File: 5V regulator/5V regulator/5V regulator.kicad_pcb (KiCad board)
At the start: 2 copper layers, 8 parts, among them J1 9V Vhod, J2 5V Izhod, U1 LM7805_TO220

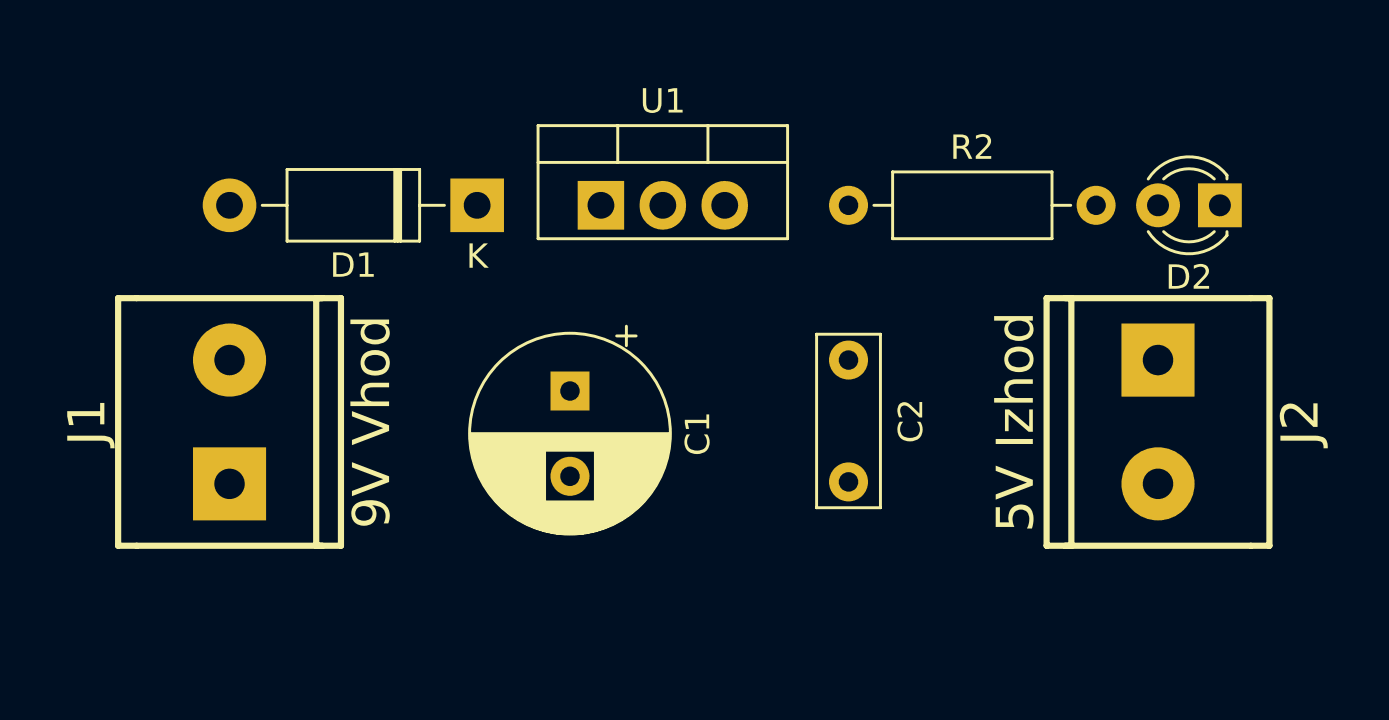
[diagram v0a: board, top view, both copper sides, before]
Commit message: 5v regulator pcb
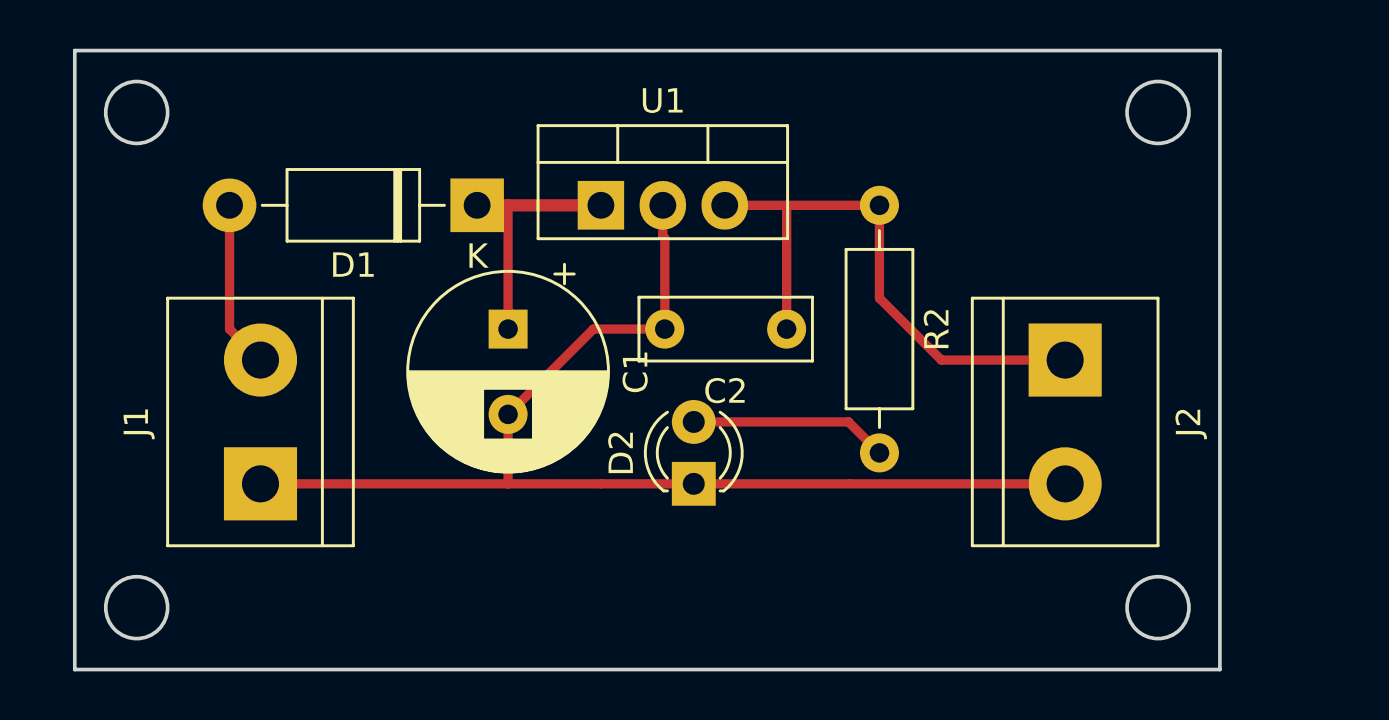
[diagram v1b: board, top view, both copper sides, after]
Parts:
- J1, J2: footprint w_conn_screw:mors_2p -> TerminalBlock:TerminalBlock_bornier-2_P5.08mm
- moved D2 24.4 mm to (144.8, 85.1), turned to 90 degrees
- moved J2 4.58 mm to (160.0, 80.0)
- moved C1 3.59 mm to (137.2, 78.7)
- moved J1 2.84 mm to (127.0, 85.1)
- moved C2 2.84 mm to (148.6, 78.7), turned to 180 degrees
- moved R2 1.27 mm to (152.4, 73.7), turned to 270 degrees
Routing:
- net Net-(C1-Pad2): track 0.00 -> 50.0 mm
- net /5V: track 0.00 -> 23.9 mm
- net Net-(C1-Pad1): track 0.00 -> 10.2 mm
- net Net-(D2-Pad2): track 0.00 -> 8.15 mm
- net /9V: track 0.00 -> 6.88 mm
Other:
- board outline added: 47 x 25.4 mm

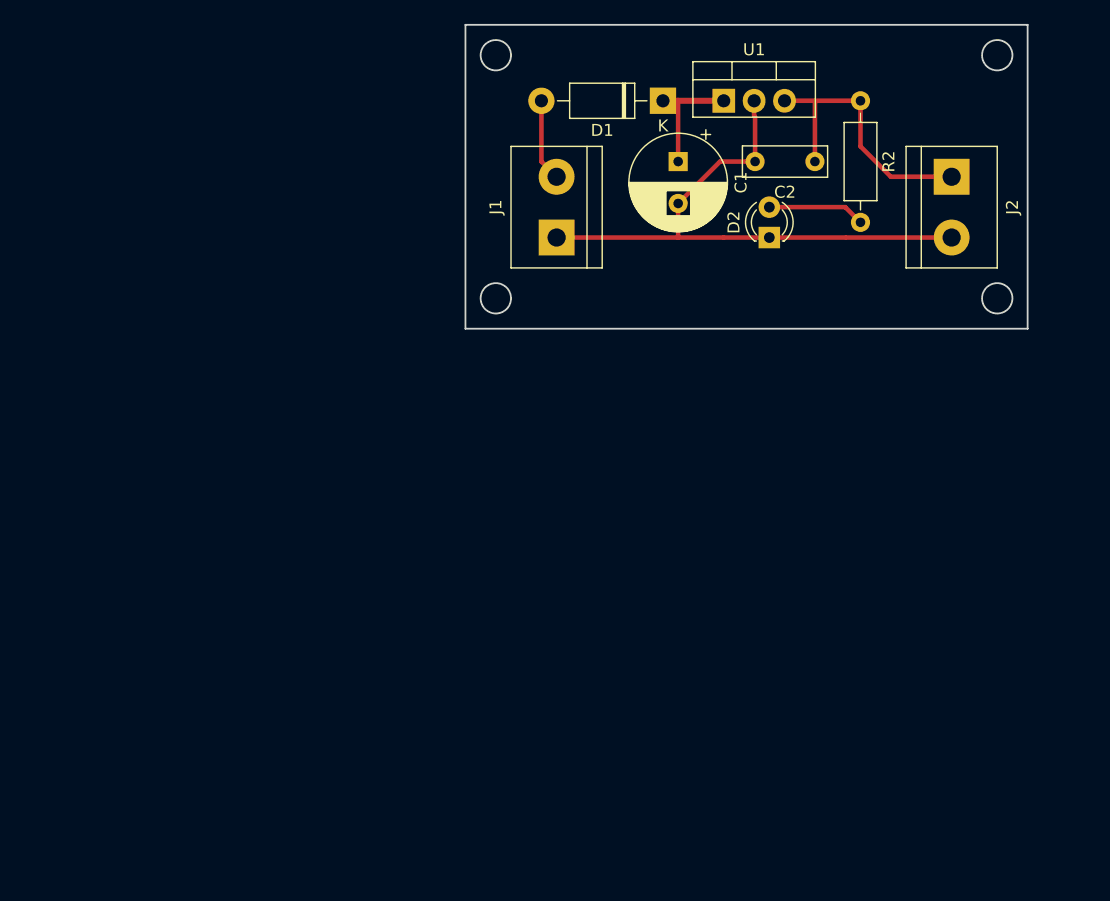
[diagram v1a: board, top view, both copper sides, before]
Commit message: updated 5v regulator
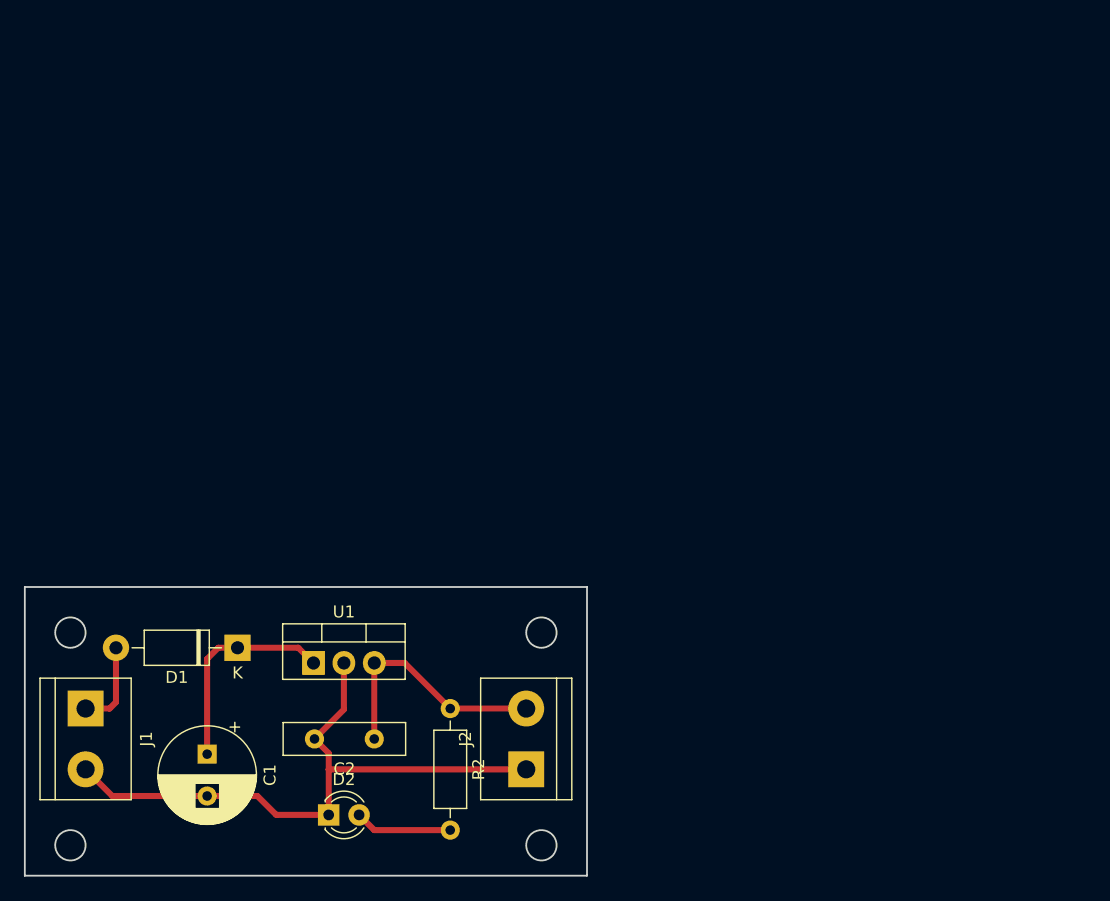
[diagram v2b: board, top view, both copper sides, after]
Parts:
- C2: footprint Capacitors_THT:C_Rect_L7.0mm_W2.5mm_P5.00mm -> Capacitor_THT:C_Disc_D10.0mm_W2.5mm_P5.00mm
- moved C1 63.3 mm to (97.8, 128.3)
- moved R2 61.3 mm to (118.1, 124.5)
- moved J2 61.0 mm to (124.5, 129.5), turned to 90 degrees
- moved C2 60.7 mm to (111.8, 127.0)
- moved D2 60.7 mm to (108.0, 133.3), turned to 0 degrees
- moved U1 58.2 mm to (106.7, 120.7)
- moved D1 57.9 mm to (100.3, 119.4)
- moved J1 55.7 mm to (87.6, 124.5), turned to 270 degrees
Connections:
- J1 pad 1: Net-(C1-Pad2) -> /9V
- J1 pad 2: /9V -> Net-(C1-Pad2)
- J2 pad 1: /5V -> Net-(C1-Pad2)
- J2 pad 2: Net-(C1-Pad2) -> /5V
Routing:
- net Net-(C1-Pad1): track 10.2 -> 17.8 mm
- net /5V: track 23.9 -> 20.6 mm
- net Net-(C1-Pad2): track 50.0 -> 52.6 mm
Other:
- board size 47 x 25.4 mm -> 47 x 24.1 mm
